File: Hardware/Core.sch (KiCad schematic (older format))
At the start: 10 parts

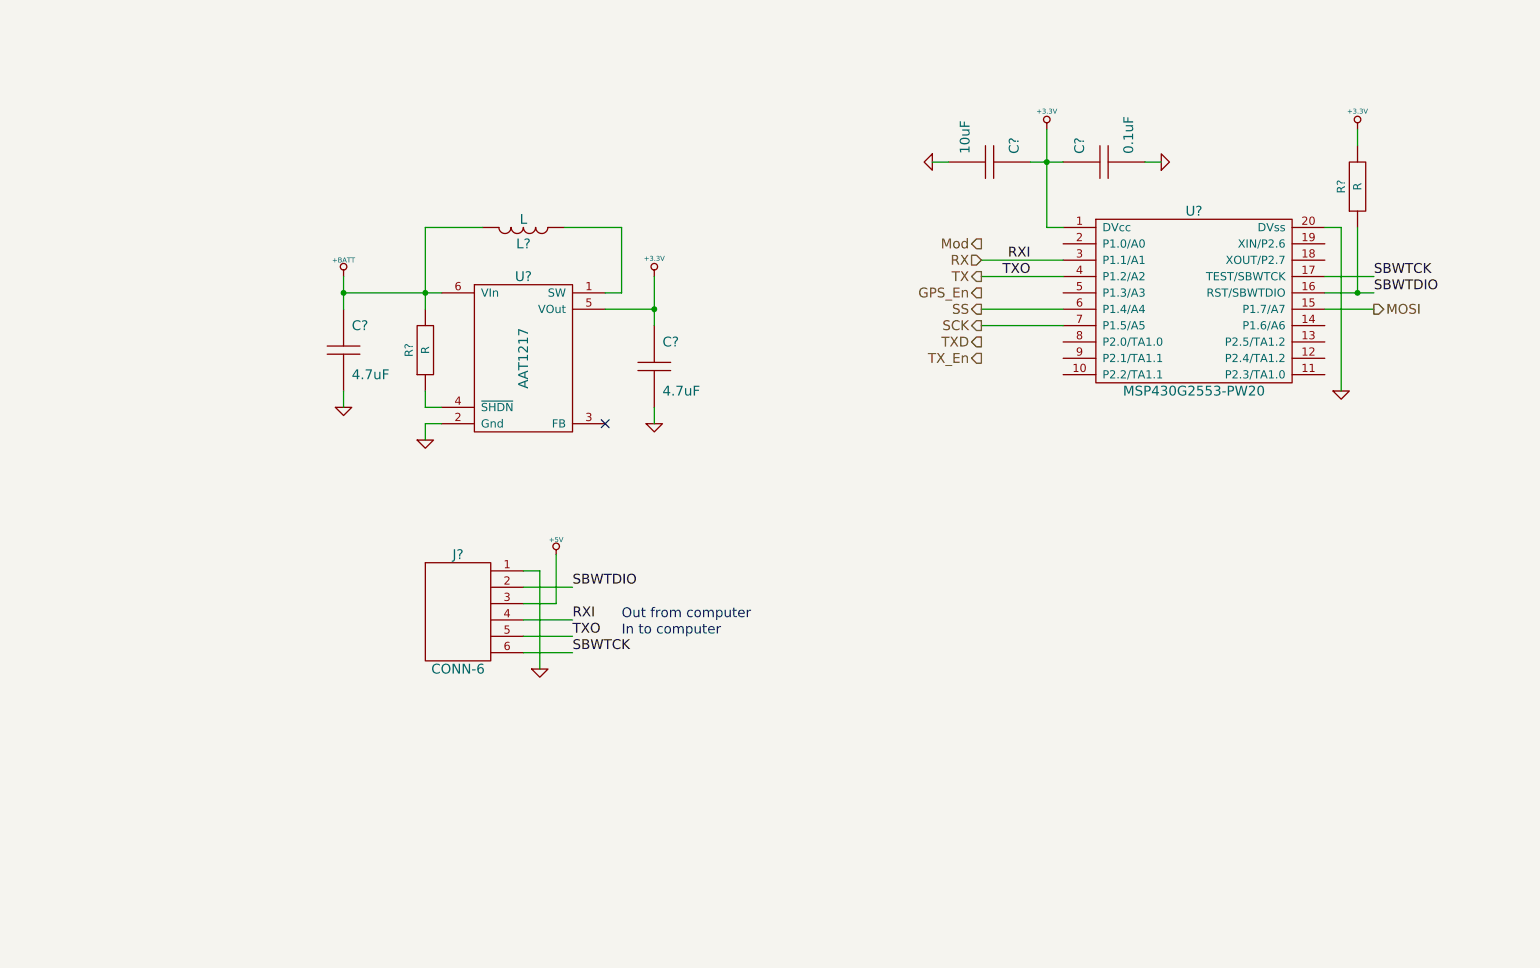
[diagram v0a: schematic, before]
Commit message: Finish modulation section
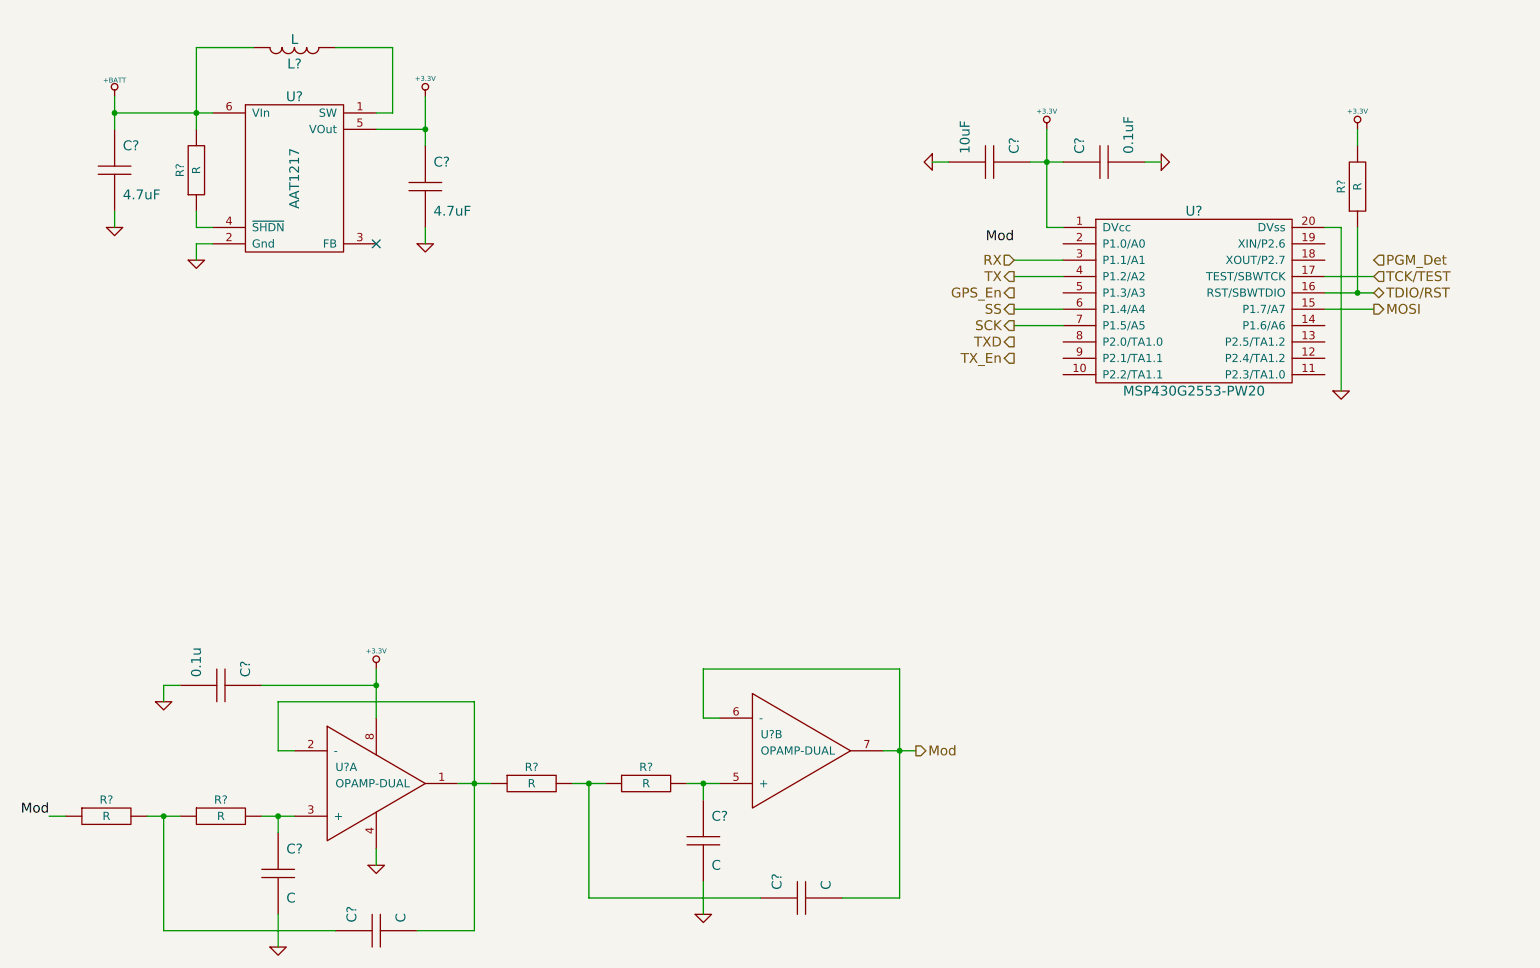
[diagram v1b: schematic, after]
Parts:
- removed J?: CONN-6, ~, symbol CONN-6
- added C? (x4): C, ~, symbol C
- added C?: 0.1u, ~, symbol C
- added R? (x4): R, ~, symbol R
- added U? (x2): OPAMP-DUAL, ~, symbol OPAMP-DUAL
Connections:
- net +3.3V: now also C?.1, U?.8
- net GND: now also C?.2, C?.2, C?.2, U?.4
- net Mod: now also C?.2, R?.1, U?.6 (-), U?.7
- net SBWTCK renamed TCK/TEST
- net SBWTDIO renamed TDIO/RST
- new net: C?.2, R?.1, U?.1, U?.2 (-)
- new net: C?.1, R?.2, U?.3 (+)
- new net: C?.1, R?.1, R?.2 (x2)
- new net: C?.1, R?.2, U?.5 (+)
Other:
- note removed: "In to computer"
- note removed: "Out from computer"
- moved on the sheet: C?, L?, R?, U?

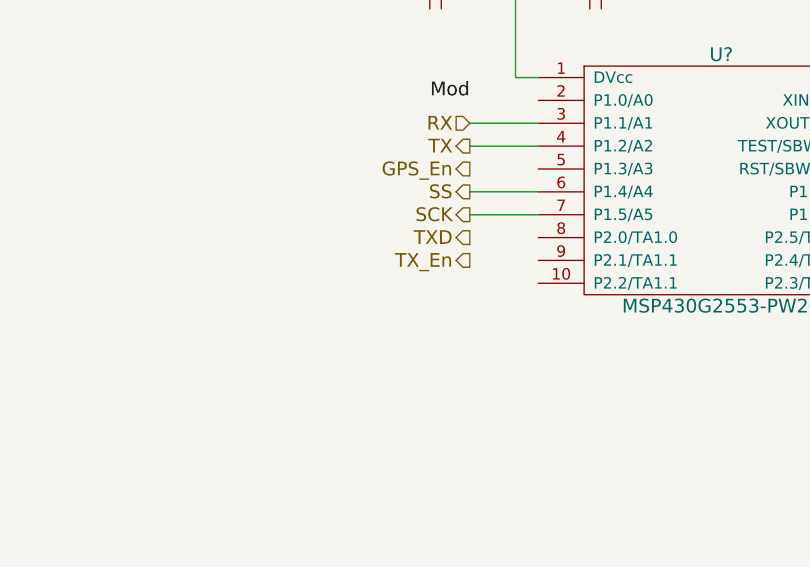
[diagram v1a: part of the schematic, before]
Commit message: Add GPS performance control
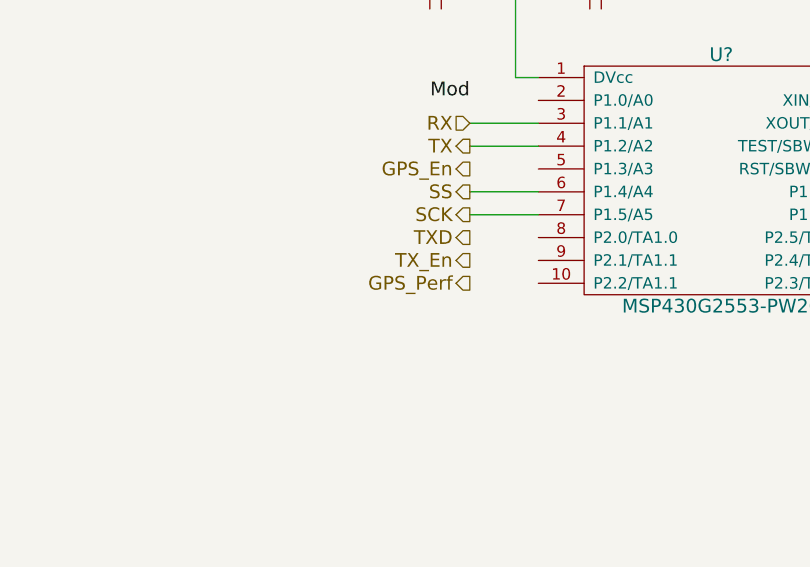
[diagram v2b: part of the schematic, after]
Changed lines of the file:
@@
 Text Label 7000 2700 2    60   ~ 0
 Mod
+Text HLabel 7000 3500 0    60   Output ~ 0
+GPS_Perf
 $EndSCHEMATC

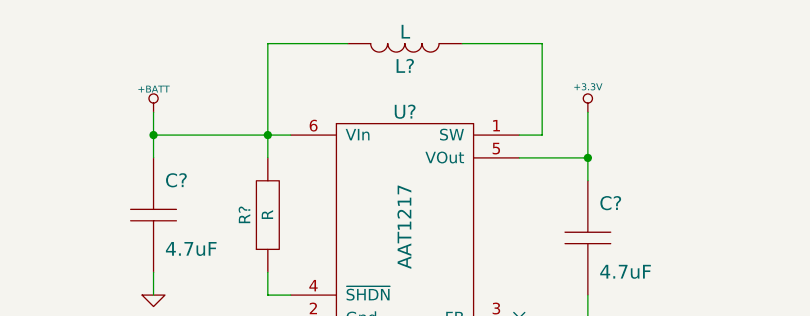
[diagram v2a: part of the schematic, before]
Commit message: Switch GPS power to main 3v3 bus
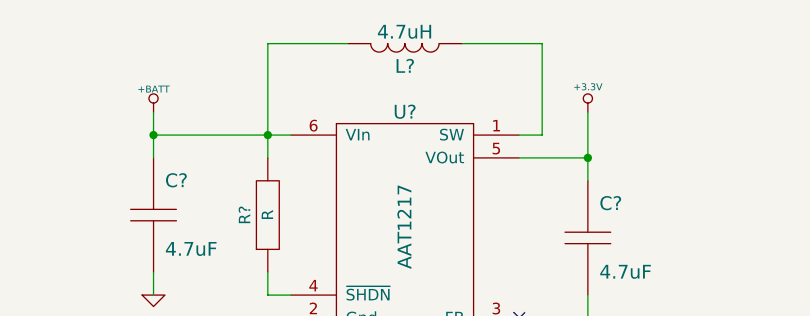
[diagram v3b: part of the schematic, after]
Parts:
- L?: value L -> 4.7uH
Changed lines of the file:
@@
 Sheet 4 4
 Title "Aether - Pico Tracker"
-Date "2 feb 2014"
+Date "3 feb 2014"
 Rev "1"
 Comp "Aerodyne Labs"
@@
 P 2600 1500
 F 0 "L?" H 2600 1400 60  0000 C CNN
-F 1 "L" H 2600 1550 60  0000 C CNN
+F 1 "4.7uH" H 2600 1550 60  0000 C CNN
 F 2 "~" H 2600 1500 60  0000 C CNN
 F 3 "~" H 2600 1500 60  0000 C CNN

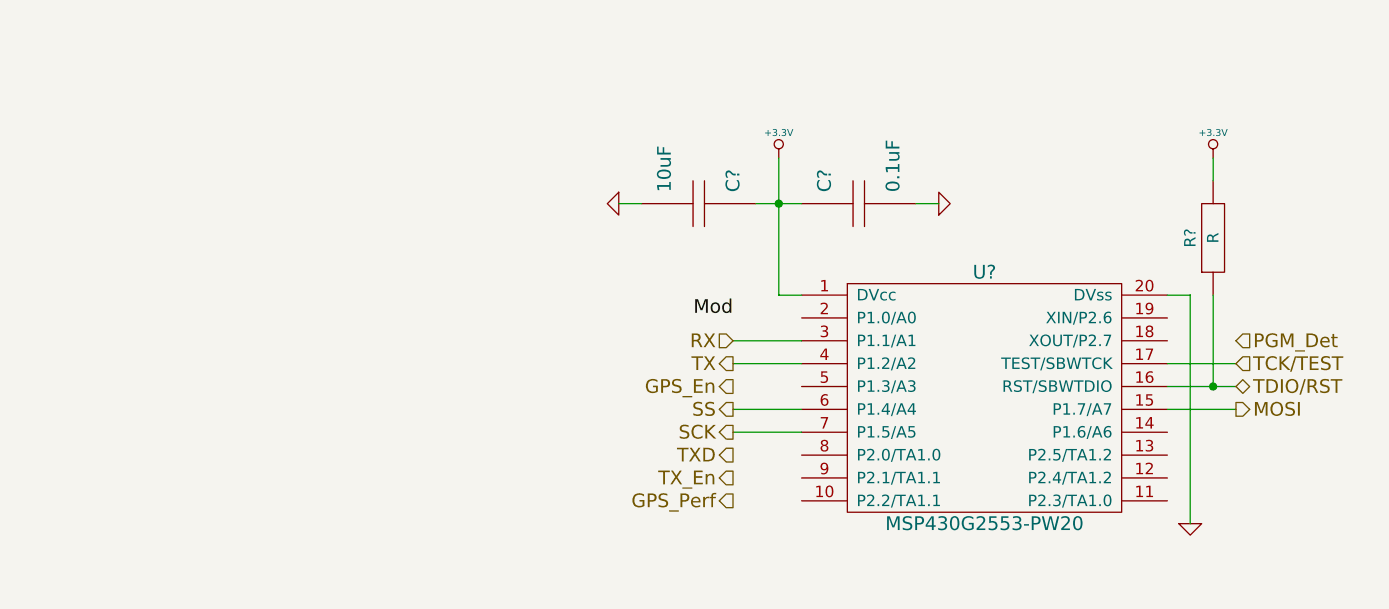
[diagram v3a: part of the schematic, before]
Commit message: Add core crystal
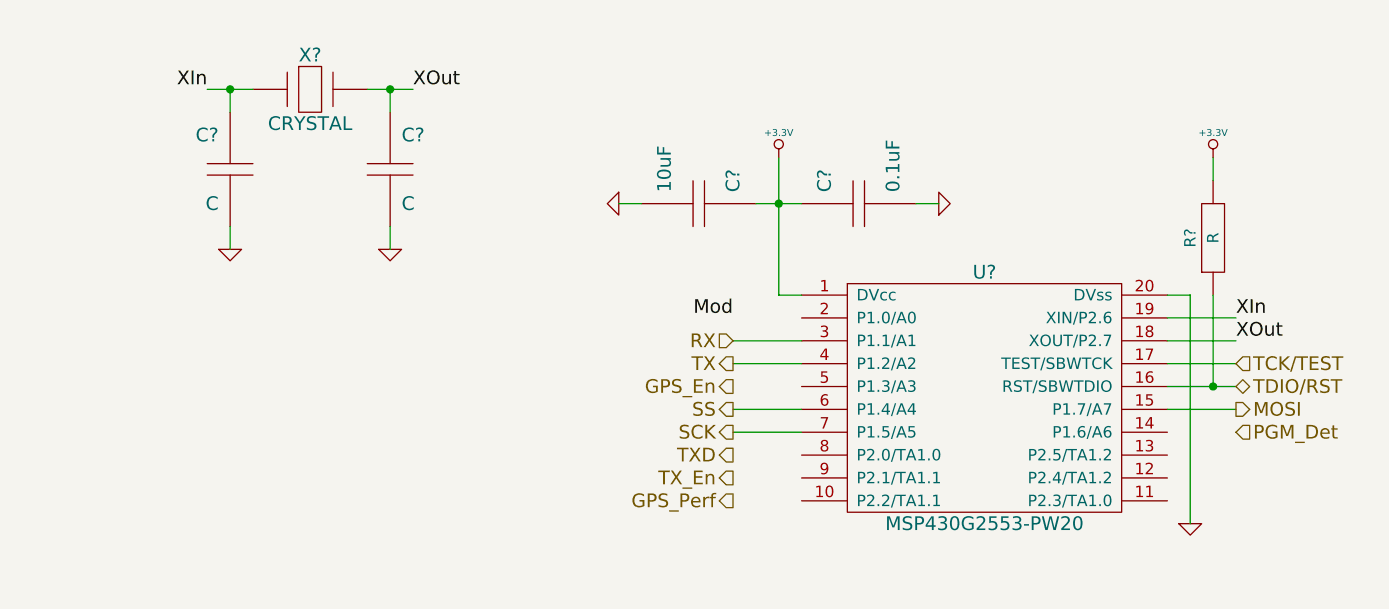
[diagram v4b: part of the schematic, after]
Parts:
- added C? (x2): C, ~, symbol C
- added X?: CRYSTAL, ~, symbol CRYSTAL
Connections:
- net GND: now also C?.2, C?.2
- net XOut: now reaches U?.18 (XOUT/P2.7)
- net XOut: now also C?.1, X?.2
- net XIn: now reaches U?.19 (XIN/P2.6)
- net XIn: now also C?.1, X?.1
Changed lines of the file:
@@
 Text HLabel 9200 2900 2    60   Input ~ 0
 TCK/TEST
-Text HLabel 9200 2800 2    60   Input ~ 0
+Text HLabel 9200 3200 2    60   Input ~ 0
 PGM_Det
 $Comp
@@
 Text HLabel 7000 3500 0    60   Output ~ 0
 GPS_Perf
+$Comp
+L CRYSTAL X?
+U 1 1 52EF2F5E
+P 5150 1700
+F 0 "X?" H 5150 1850 60  0000 C CNN
+F 1 "CRYSTAL" H 5150 1550 60  0000 C CNN
+F 2 "~" H 5150 1700 60  0000 C CNN
+F 3 "~" H 5150 1700 60  0000 C CNN
+	1    5150 1700
+	1    0    0    -1
+$EndComp
+$Comp
+L C C?
+U 1 1 52EF2F6D
+P 5500 2050
+F 0 "C?" H 5550 2200 60  0000 L CNN
+F 1 "C" H 5550 1900 60  0000 L CNN
+F 2 "~" H 5500 2050 60  0000 C CNN
+F 3 "~" H 5500 2050 60  0000 C CNN
+F 4 "V" H 5450 1900 60  0001 R CNN "Voltage"
+F 5 "D" H 5450 2200 60  0001 R CNN "Dielectric"
+	1    5500 2050
+	1    0    0    -1
+$EndComp
+$Comp
+L C C?
+U 1 1 52EF2F88
+P 4800 2050
+F 0 "C?" H 4850 2200 60  0000 L CNN
+F 1 "C" H 4850 1900 60  0000 L CNN
+F 2 "~" H 4800 2050 60  0000 C CNN
+F 3 "~" H 4800 2050 60  0000 C CNN
+F 4 "V" H 4750 1900 60  0001 R CNN "Voltage"
+F 5 "D" H 4750 2200 60  0001 R CNN "Dielectric"
+	1    4800 2050
+	-1   0    0    -1
+$EndComp
+Text Label 5600 1700 0    60   ~ 0
+XOut
+Text Label 4700 1700 2    60   ~ 0
+XIn
+Wire Wire Line
+	4700 1700 4900 1700
+Wire Wire Line
+	5400 1700 5600 1700
+Wire Wire Line
+	5500 1800 5500 1700
+Connection ~ 5500 1700
+Wire Wire Line
+	4800 1800 4800 1700
+Connection ~ 4800 1700
+$Comp
+L GND #PWR?
+U 1 1 52EF30D2
+P 5500 2400
+F 0 "#PWR?" H 5500 2400 30  0001 C CNN
+F 1 "GND" H 5500 2330 30  0001 C CNN
+F 2 "" H 5500 2400 60  0000 C CNN
+F 3 "" H 5500 2400 60  0000 C CNN
+	1    5500 2400
+	1    0    0    -1
+$EndComp
+$Comp
+L GND #PWR?
+U 1 1 52EF30E1
+P 4800 2400
+F 0 "#PWR?" H 4800 2400 30  0001 C CNN
+F 1 "GND" H 4800 2330 30  0001 C CNN
+F 2 "" H 4800 2400 60  0000 C CNN
+F 3 "" H 4800 2400 60  0000 C CNN
+	1    4800 2400
+	1    0    0    -1
+$EndComp
+Wire Wire Line
+	4800 2400 4800 2300
+Wire Wire Line
+	5500 2300 5500 2400
+Text Label 9200 2700 0    60   ~ 0
+XIn
+Text Label 9200 2800 0    60   ~ 0
+XOut
+Wire Wire Line
+	8900 2700 9200 2700
+Wire Wire Line
+	8900 2800 9200 2800
 $EndSCHEMATC
